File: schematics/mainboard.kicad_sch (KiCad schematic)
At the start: 2 parts

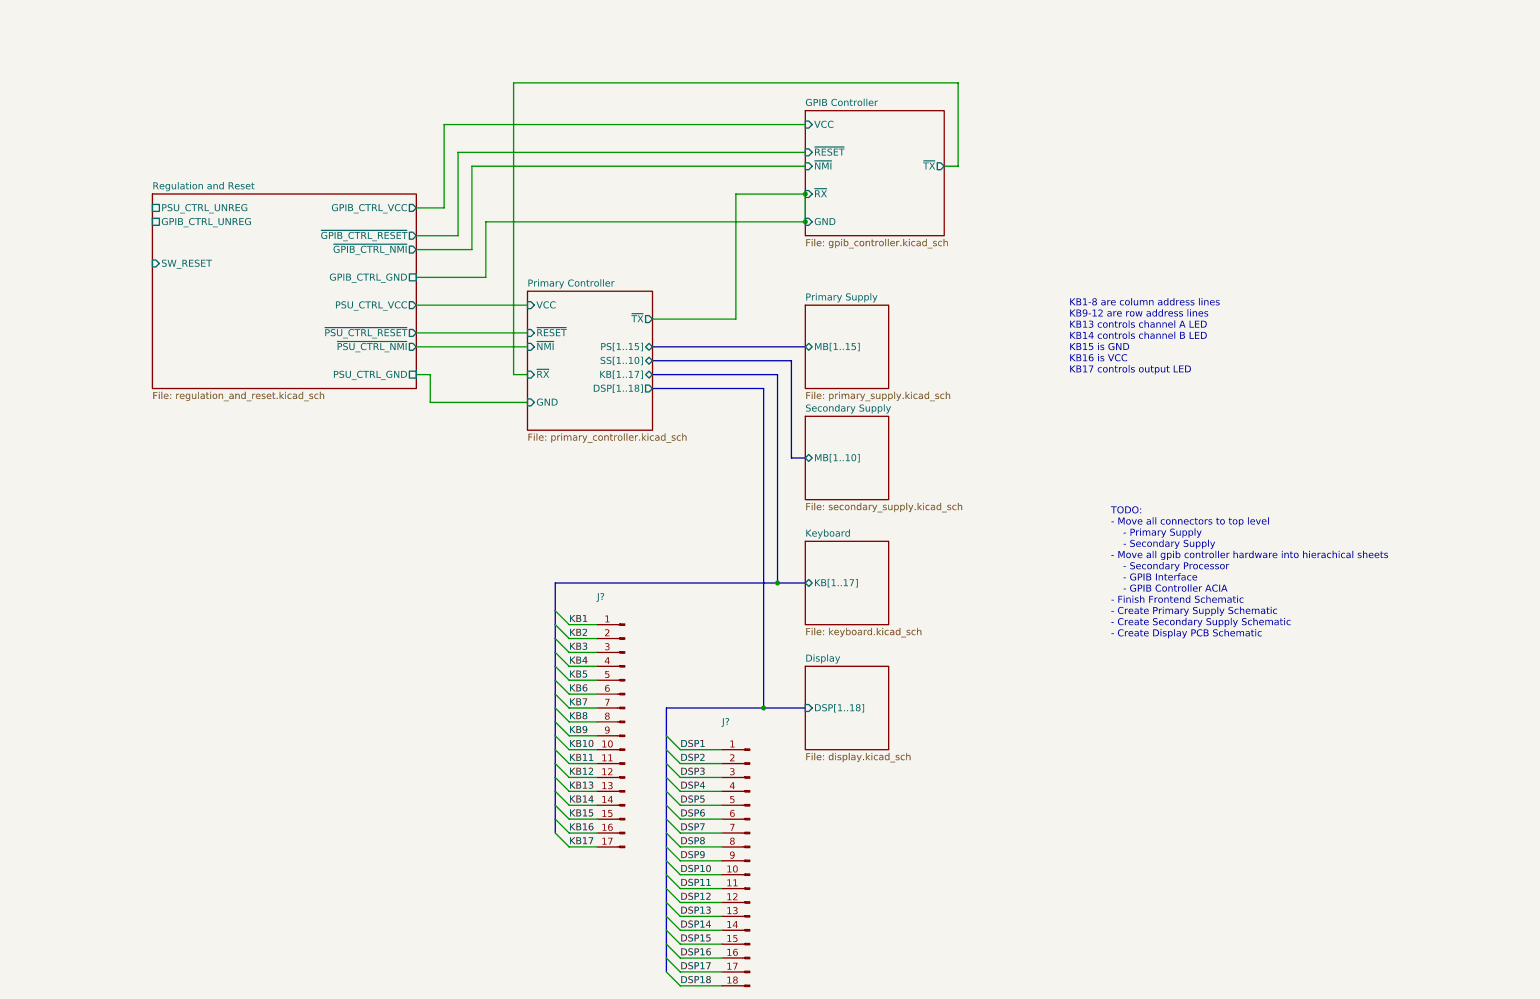
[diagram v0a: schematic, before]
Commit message: Moved more components into hierachical sheets, misc cleanup
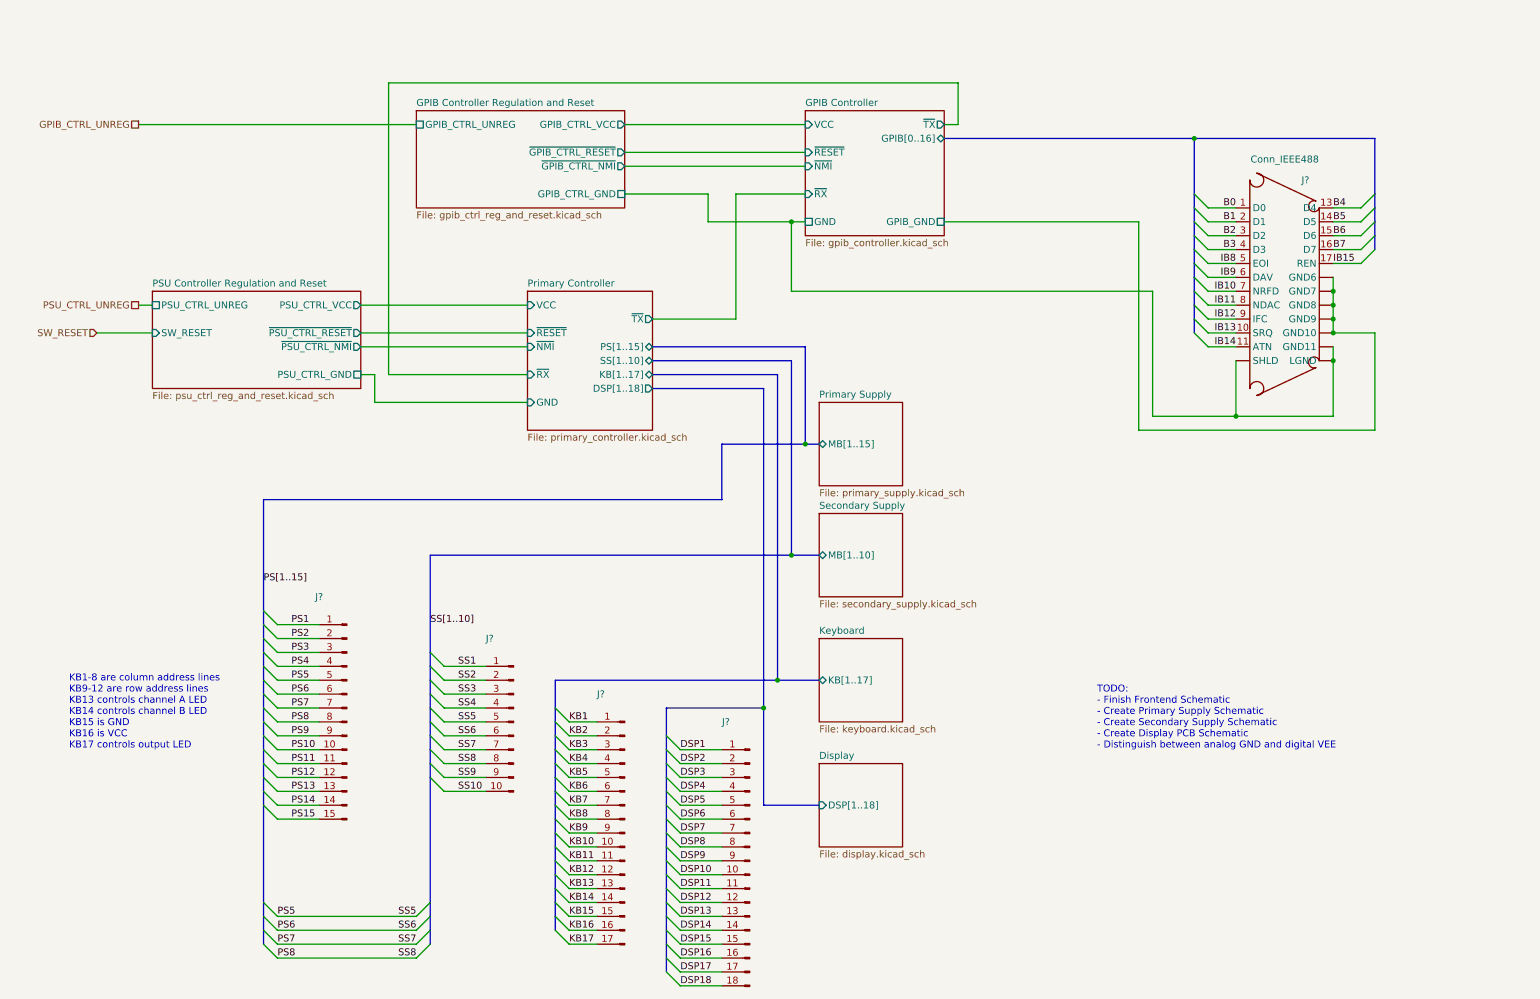
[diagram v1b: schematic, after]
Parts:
- added J?: ~, symbol Connector:Conn_01x15_Male
- added J?: Conn_IEEE488, symbol Custom:Conn_IEEE488
- added J?: ~, symbol Connector:Conn_01x10_Male
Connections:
- new net B0: J?.1 (D0)
- new net B1: J?.2 (D1)
- new net B2: J?.3 (D2)
- new net B3: J?.4 (D3)
- new net B4: J?.13 (D4)
- new net B5: J?.14 (D5)
- new net B6: J?.15 (D6)
- new net B7: J?.16 (D7)
- new net GPIB Controller Regulation and Reset/GPIB_CTRL_GND: J?. (SHLD)
- new net GPIB Controller/GPIB_GND: J?. (SHLD)
- new net IB10: J?.7 (NRFD)
- new net IB11: J?.8 (NDAC)
- new net IB12: J?.9 (IFC)
- new net IB13: J?.10 (SRQ)
- new net IB14: J?.11 (ATN)
- new net IB15: J?.17 (REN)
- new net IB8: J?.5 (EOI)
- new net IB9: J?.6 (DAV)
- new net PS1: J?.1 (Pin_1)
- new net PS10: J?.10 (Pin_10)
- new net PS11: J?.11 (Pin_11)
- new net PS12: J?.12 (Pin_12)
- new net PS13: J?.13 (Pin_13)
- new net PS14: J?.14 (Pin_14)
- new net PS15: J?.15 (Pin_15)
- new net PS2: J?.2 (Pin_2)
- new net PS3: J?.3 (Pin_3)
- new net PS4: J?.4 (Pin_4)
- new net PS5: J?.5 (Pin_5), J?.5 (Pin_5)
- new net PS6: J?.6 (Pin_6), J?.6 (Pin_6)
- new net PS7: J?.7 (Pin_7), J?.7 (Pin_7)
- new net PS8: J?.8 (Pin_8), J?.8 (Pin_8)
- new net PS9: J?.9 (Pin_9)
- new net SS1: J?.1 (Pin_1)
- new net SS10: J?.10 (Pin_10)
- new net SS2: J?.2 (Pin_2)
- new net SS3: J?.3 (Pin_3)
- new net SS4: J?.4 (Pin_4)
- new net SS9: J?.9 (Pin_9)
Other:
- removed sheet Regulation and Reset
- added sheet GPIB Controller Regulation and Reset (gpib_ctrl_reg_and_reset.kicad_sch)
- added sheet PSU Controller Regulation and Reset (psu_ctrl_reg_and_reset.kicad_sch)
- sheet GPIB Controller ports: added GPIB[0..16], GPIB_GND; removed none
- note added: "TODO: - Finish Frontend Schematic - Create Primary Supply Schematic - Create Secondary Supply Schematic - Create Display PCB Schematic - Distinguish between analog GND and digital VEE"
- note removed: "TODO: - Move all connectors to top level - Primary Supply - Secondary Supply - Move all gpib controller hardware into hierachical sheets - Secondary Processor - GPIB Interface - GPIB Controller ACIA - Finish Frontend Schematic - Create Primary Supply Schematic - Create Secondary Supply Schematic - Create Display PCB Schematic"
- moved on the sheet: J?

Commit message: cleanup, fixes, started on power supplies
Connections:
- net IB10 renamed B10
- net IB11 renamed B11
- net IB12 renamed B12
- net IB13 renamed B13
- net IB14 renamed B14
- net IB15 renamed B15
- net IB8 renamed B8
- net IB9 renamed B9
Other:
- added sheet ACIA Isolation (acia_isolation.kicad_sch)
- note added: "TODO: - Finish Frontend Schematic - Create Primary Supply Schematic - Create Secondary Supply Schematic - Create Display PCB Schematic - Finish Cleanup"
- note removed: "TODO: - Finish Frontend Schematic - Create Primary Supply Schematic - Create Secondary Supply Schematic - Create Display PCB Schematic - Distinguish between analog GND and digital VEE"
- moved on the sheet: J?

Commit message: More power supply work
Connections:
- net PS5 renamed AV+
- net PS6 renamed AV-
- net PS7 renamed GND
- net PS8 renamed OEN
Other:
- sheet Primary Controller ports: added AVCC, AVEE, SW_RST; removed none
- sheet Primary Supply ports: added PS[1..15]; removed MB[1..15]
- sheet Secondary Supply ports: added SS[1..10]; removed MB[1..10]

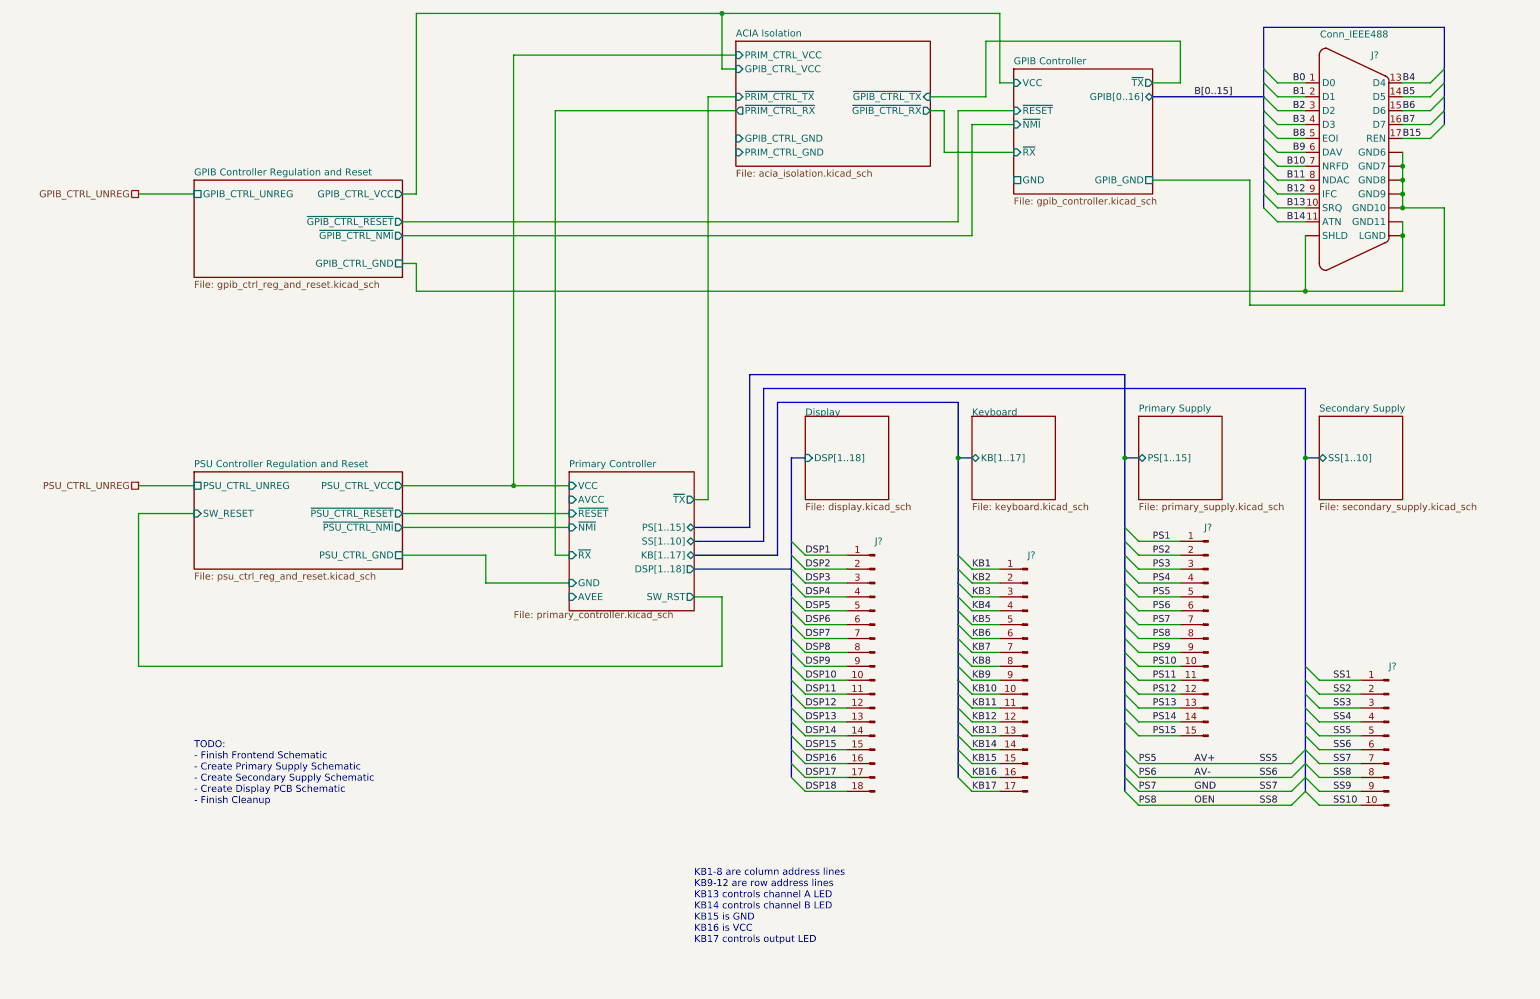
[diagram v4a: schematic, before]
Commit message: Updated to KiCad v10.0. Minor improvements.
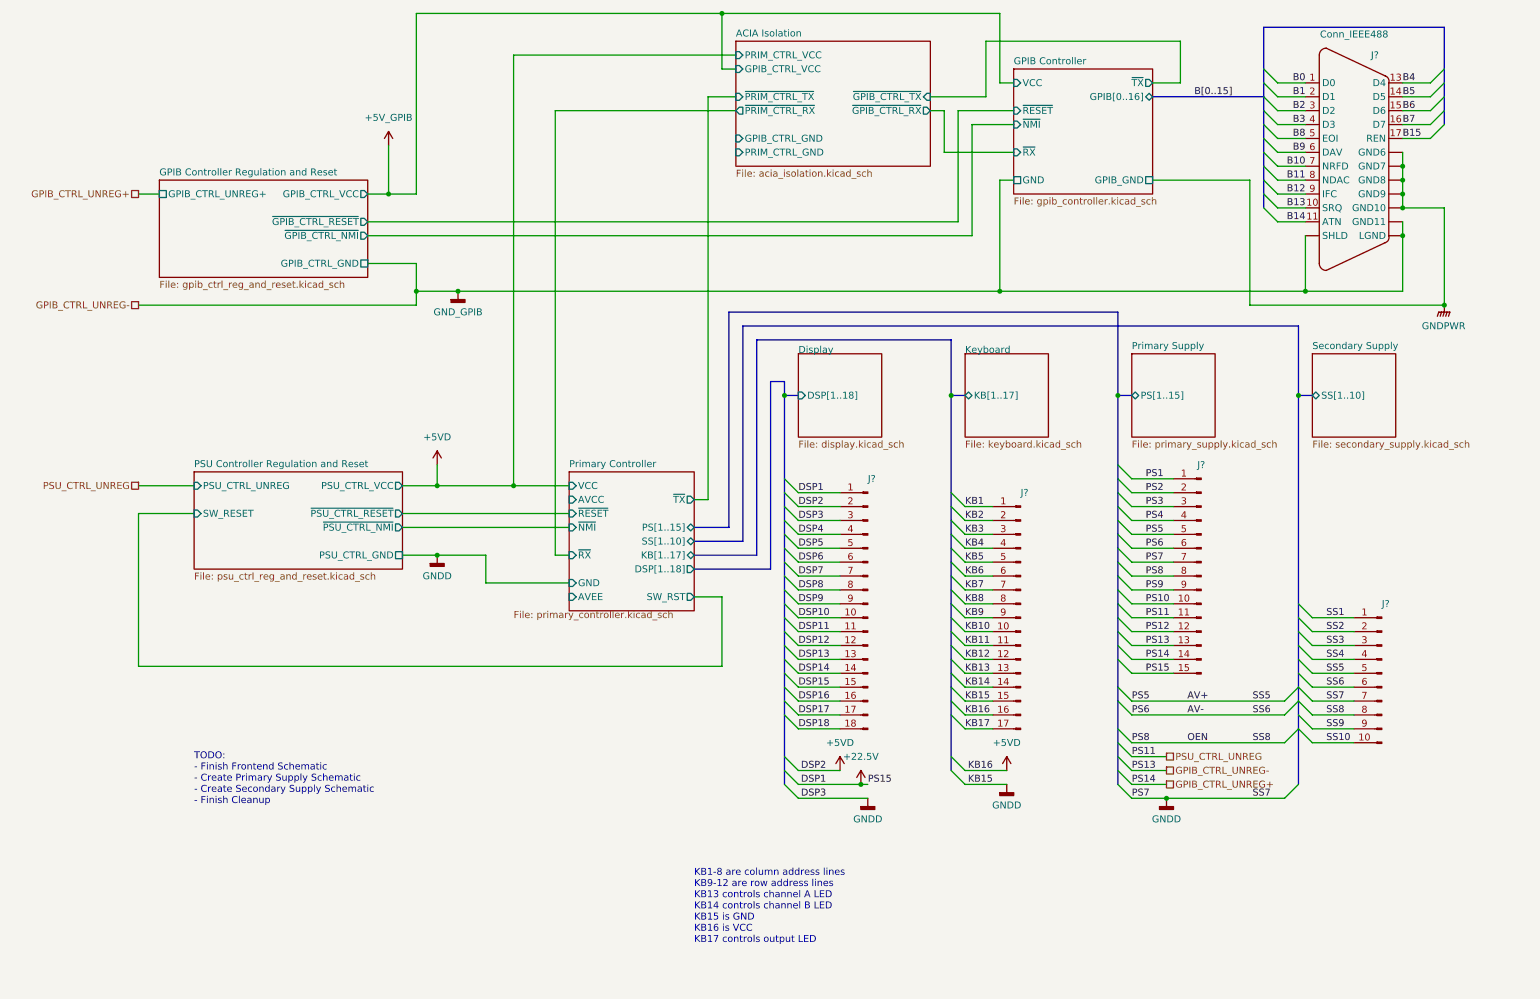
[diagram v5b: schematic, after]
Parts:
- J? (x4): value ~ -> (none)
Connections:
- net GND is gone; now on net GNDD: J?.7 (Pin_7), J?.7 (Pin_7)
- net GPIB Controller/GPIB_GND is gone; now on net GND_GPIB: J?. (LGND)
- net KB15 is gone; now on net GNDD: J?.15 (Pin_15)
- net KB16 is gone; now on net +5VD: J?.16 (Pin_16)
- net PS11 is gone; now on net PSU_CTRL_UNREG: J?.11 (Pin_11)
- net PS13 is gone; now on net GND_GPIB: J?.13 (Pin_13)
- net PS15 is gone; now on net +22.5V: J?.15 (Pin_15)
- net DSP1 renamed +22.5V
- net DSP2 renamed +5VD
- net DSP3 renamed GNDD
- net GPIB Controller Regulation and Reset/GPIB_CTRL_GND renamed GND_GPIB
- net PS14 renamed GPIB_CTRL_UNREG+
- new net GNDPWR: J?. (LGND)
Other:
- sheet GPIB Controller Regulation and Reset ports: added GPIB_CTRL_UNREG+; removed GPIB_CTRL_UNREG
- note added: "TODO: - Finish Frontend Schematic - Create Primary Supply Schematic - Create Secondary Supply Schematic - Finish Cleanup"
- note removed: "TODO: - Finish Frontend Schematic - Create Primary Supply Schematic - Create Secondary Supply Schematic - Create Display PCB Schematic - Finish Cleanup"
- moved on the sheet: J?
